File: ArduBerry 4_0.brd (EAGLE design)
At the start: 50.9 x 60.9 mm, 30 parts, among them J1 AVR_SPI_PRG_62X3_LOCK, J2 POWER_JACKPTH_LOCK, Q3 MOSFET-N-044020001, Q4 MOSFET-N-044020001, U1 ATMEGA328P_PDIP, U2 ARDUINO_SHIELDNO_SILK

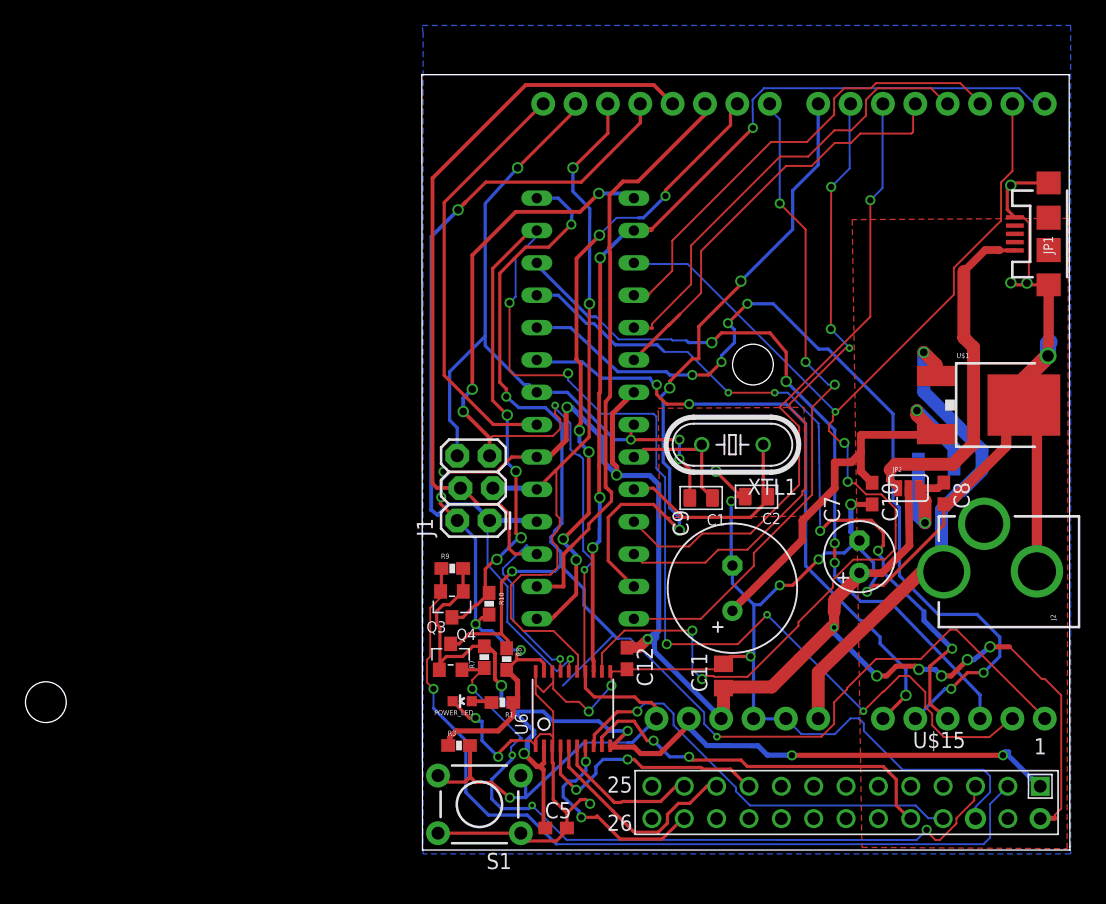
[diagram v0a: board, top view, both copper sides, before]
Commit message: Rounded the edges
Rounded the edges of the board a bit.  Looks nicer.
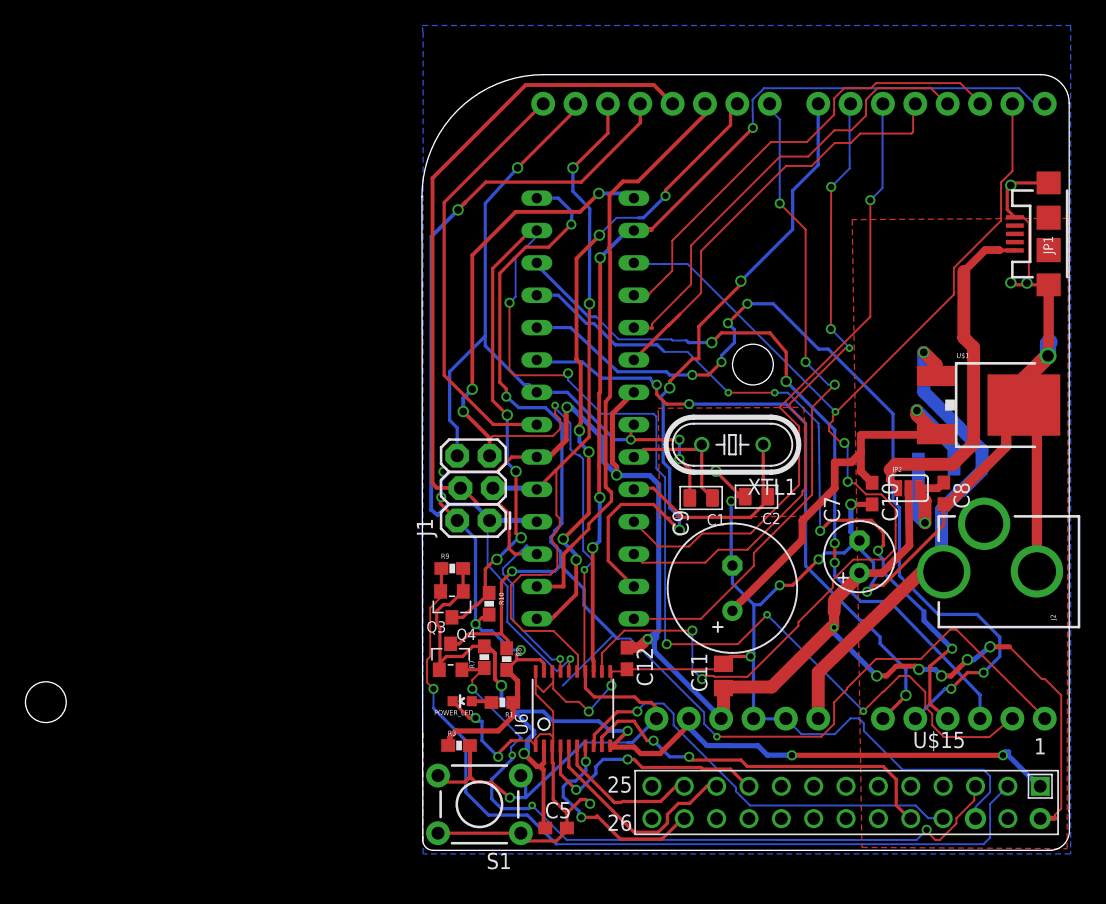
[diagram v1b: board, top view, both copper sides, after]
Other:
- board size 50.9 x 60.9 mm -> 50.8 x 60.9 mm
